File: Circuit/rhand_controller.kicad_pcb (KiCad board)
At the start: 2 copper layers, 100 x 100 mm, 37 parts, among them P1 Wall, P10 LW_ADC, P11 RU_ADC, P12 RV_ADC, P13 RW_ADC, P17 CONN_01X06, P2 CW, P3 Enable, P4 CCW, P5 LW_ADC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

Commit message: 部品割り付けの完了
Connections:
- P5 pad 2: /RHand/Joy_X -> /Joy_X
- P6 pad 2: /RHand/Joy_Y -> /Joy_Y
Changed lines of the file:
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@@
-(kicad_pcb (version 4) (host pcbnew 4.0.5)
+(kicad_pcb (version 4) (host pcbnew 4.0.6)
   (general
-    (links 121)
-    (no_connects 99)
+    (links 123)
+    (no_connects 101)
     (area 49.924999 69.924999 150.075001 170.075001)
     (thickness 1.6)
@@
     (zones 0)
     (modules 37)
-    (nets 59)
+    (nets 57)
   )
   (page A4)
@@
   (net 54 "Net-(U2-Pad26)")
   (net 55 "Net-(U3-Pad4)")
-  (net 56 /RHand/Joy_X)
-  (net 57 /RHand/Joy_Y)
-  (net 58 "Net-(SW2-Pad3)")
+  (net 56 "Net-(SW2-Pad3)")
   (net_class Default "これは標準のネット クラスです。"
     (clearance 0.2)
@@
     (add_net /LeftW)
     (add_net /NRST)
-    (add_net /RHand/Joy_X)
-    (add_net /RHand/Joy_Y)
     (add_net /RightU)
     (add_net /RightV)
@@
       (net 2 GND))
     (pad 2 thru_hole circle (at -2.5 0 90) (size 1.2 1.2) (drill 0.8) (layers *.Cu *.Mask F.SilkS)
-      (net 56 /RHand/Joy_X))
+      (net 11 /Joy_X))
     (pad 3 thru_hole circle (at -5 0 90) (size 1.2 1.2) (drill 0.8) (layers *.Cu *.Mask F.SilkS)
       (net 3 +3V3))
@@
       (net 2 GND))
     (pad 2 thru_hole circle (at -2.5 0 90) (size 1.2 1.2) (drill 0.8) (layers *.Cu *.Mask F.SilkS)
-      (net 57 /RHand/Joy_Y))
+      (net 12 /Joy_Y))
     (pad 3 thru_hole circle (at -5 0 90) (size 1.2 1.2) (drill 0.8) (layers *.Cu *.Mask F.SilkS)
       (net 3 +3V3))
@@
       (net 1 "Net-(BT1-Pad1)"))
     (pad 3 thru_hole circle (at 2.54 0 270) (size 2.2 2.2) (drill 1.016) (layers *.Cu *.Mask F.SilkS)
-      (net 58 "Net-(SW2-Pad3)"))
+      (net 56 "Net-(SW2-Pad3)"))
     (model pin_array/pins_array_5x1.wrl
       (at (xyz 0 0 0))

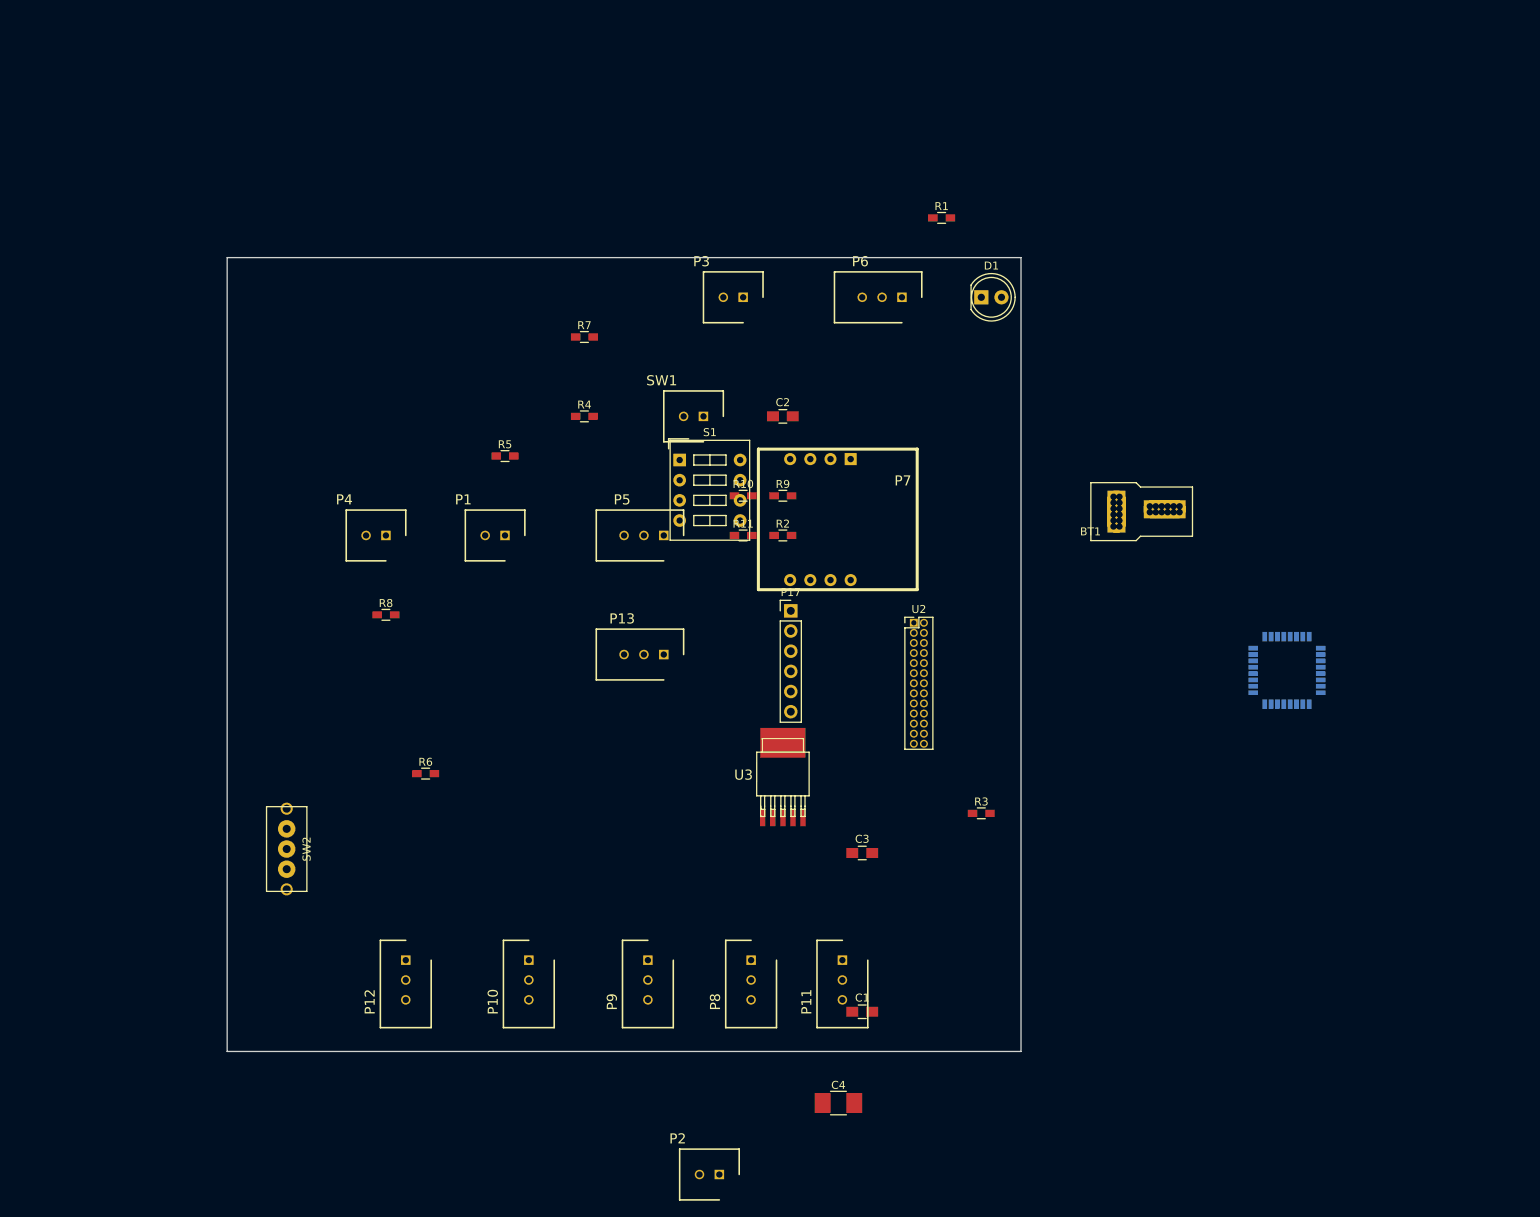
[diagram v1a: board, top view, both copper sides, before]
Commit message: 部品を基板上へ適当に配置
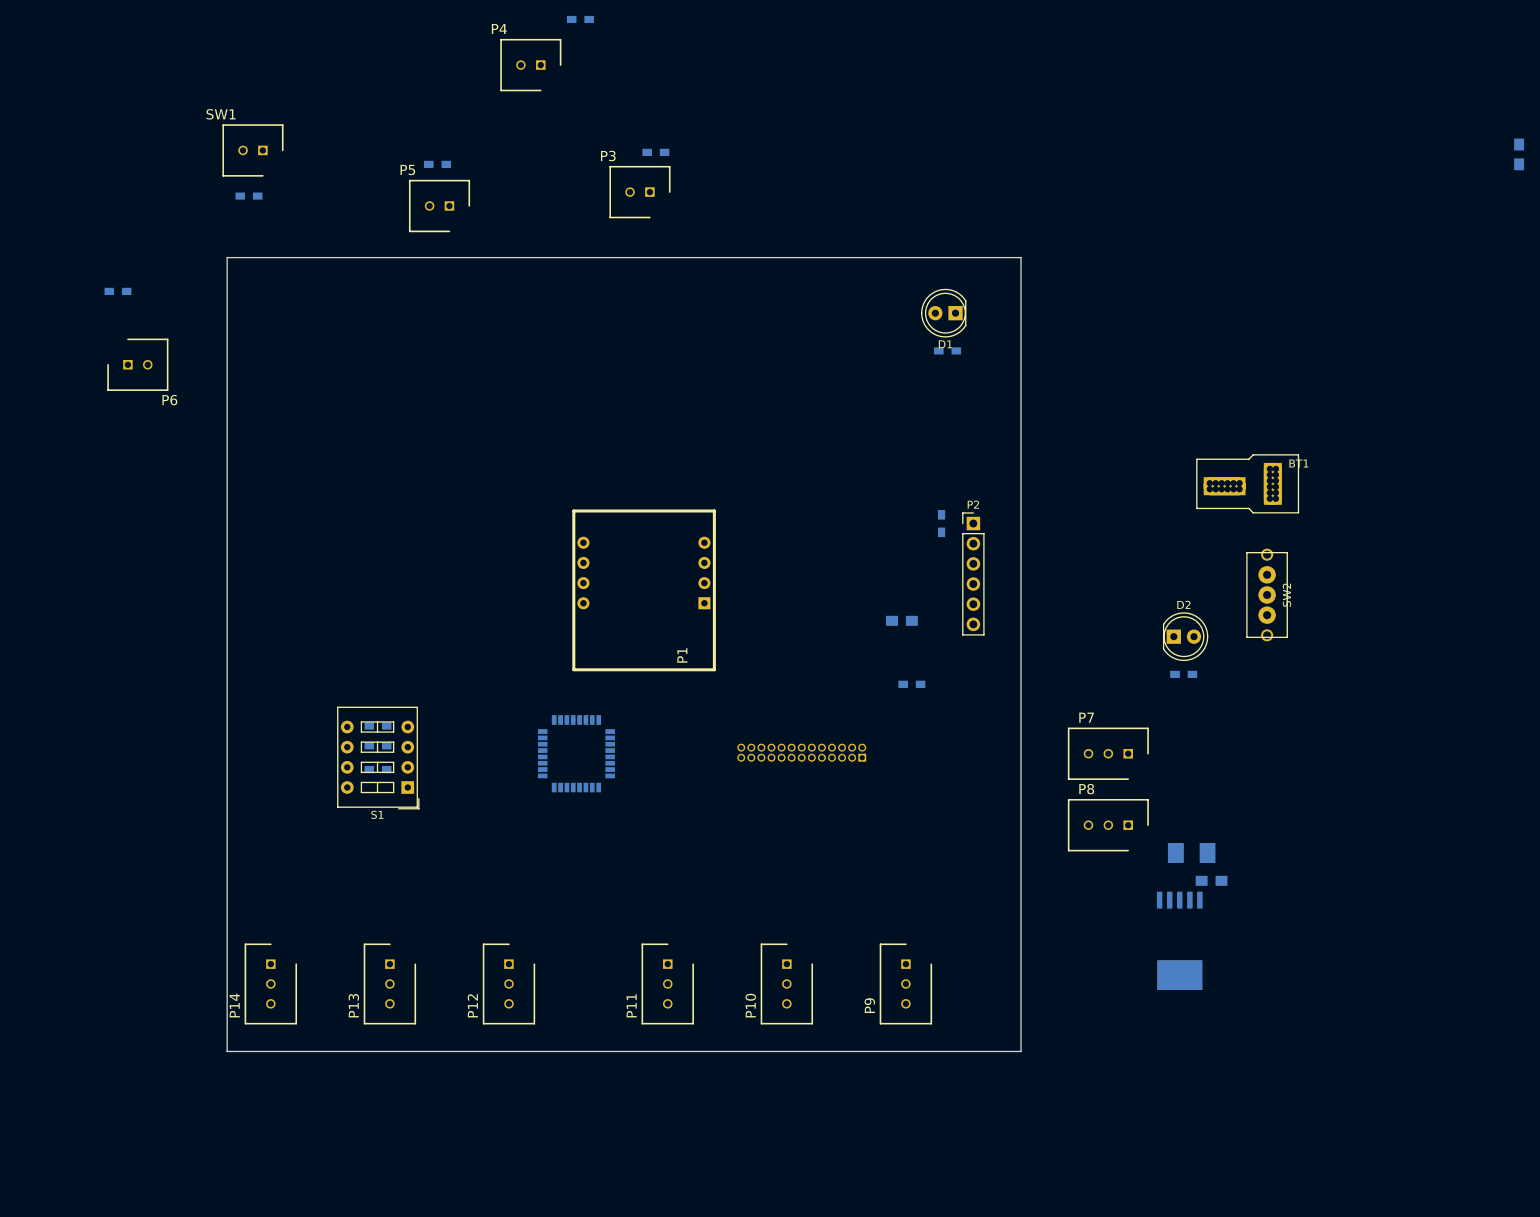
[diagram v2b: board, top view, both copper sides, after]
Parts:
- removed P17: CONN_01X06, Pin_Headers:Pin_Header_Straight_1x06_Pitch2.54mm
- added D2: LED, LEDs:LED_D5.0mm, F.Cu at (169.2, 117.8)
- added P14: RW_ADC, YASU:XA_3Pin, F.Cu at (55.5, 159.0)
- added R12: 1k, Resistors_SMD:R_0603_HandSoldering, B.Cu at (170.5, 122.5)
- BT1: value Battery -> Battery_Cell
- C1, C2, C3, C4, R10, R11, R2, R4, R6, R8, R9, U3: moved to B.Cu
- P1: value Wall -> BLUETOOTH; footprint YASU:XA_2Pin -> robocon_pcb:ESD200
- P10: value LW_ADC -> LV_ADC
- P11: value RU_ADC -> LW_ADC
- P12: value RV_ADC -> RU_ADC
- P13: value RW_ADC -> RV_ADC
- P2: value CW -> CONN_01X06; footprint YASU:XA_2Pin -> Pin_Headers:Pin_Header_Straight_1x06_Pitch2.54mm
- P3: value Enable -> Wall
- P4: value CCW -> CW
- P5: value LW_ADC -> Enable; footprint YASU:XA_3Pin -> YASU:XA_2Pin
- P6: value RW_ADC -> CCW; footprint YASU:XA_3Pin -> YASU:XA_2Pin
- P7: value BLUETOOTH -> JoyX; footprint robocon_pcb:ESD200 -> YASU:XA_3Pin
- P8: value LU_ADC -> JoyY
- P9: value LV_ADC -> LU_ADC
- R1, R3: value 1k -> 10k; moved to B.Cu
- R5, R7: value 10k -> 1k; moved to B.Cu
- U1: value STM32F042 -> IM315TRX; footprint Housings_QFP:LQFP-32_7x7mm_Pitch0.8mm -> Pin_Headers:Pin_Header_Straight_2x13_Pitch1.27mm
- U2: value IM315TRX -> STM32F042; footprint Pin_Headers:Pin_Header_Straight_2x13_Pitch1.27mm -> Housings_QFP:LQFP-32_7x7mm_Pitch0.8mm; moved to B.Cu
- moved C1 136.1 mm to (212.8, 57.0), turned to 270 degrees
- moved SW2 127.6 mm to (181.0, 112.5)
- moved P6 97.9 mm to (37.5, 83.5), turned to 180 degrees
- moved R1 95.6 mm to (69.0, 129.0), turned to 180 degrees
- moved P2 88.0 mm to (144.0, 103.5)
- moved R11 84.5 mm to (36.2, 74.2)
- moved R3 76.2 mm to (69.0, 134.5), turned to 180 degrees
- moved R8 67.4 mm to (104.0, 56.8), turned to 180 degrees
- moved R9 65.2 mm to (94.5, 40.0)
- moved SW1 64.8 mm to (54.5, 56.5)
- moved P4 62.4 mm to (89.5, 45.8)
- moved R6 62.3 mm to (136.2, 123.8), turned to 180 degrees
- moved R2 57.5 mm to (69.0, 131.5), turned to 180 degrees
- moved R5 57.3 mm to (140.8, 81.8), turned to 180 degrees
- moved R10 56.8 mm to (76.5, 58.2), turned to 180 degrees
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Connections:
- C1 pad 1: +3V3 -> GND
- C1 pad 2: GND -> +3V3
- C2 pad 1: GND -> +3V3
- C2 pad 2: +3V3 -> GND
- P1 pad 2: /Wall -> +3V3
- P10 pad 2: /LeftW -> /LeftV
- P11 pad 2: /RightV -> /LeftW
- P12 pad 2: /RightW -> /RightU
- P13 pad 2: /RightU -> /RightV
- P2 pad 1: GND -> Net-(P2-Pad1)
- P2 pad 2: /CW -> /SWCLK
- P3 pad 2: /Enable -> /Wall
- P4 pad 2: /CCW -> /CW
- P5 pad 2: /Joy_X -> /Enable
- P6 pad 2: /Joy_Y -> /CCW
- P7 pad 2: +3V3 -> /Joy_X
- P7 pad 3: Net-(P7-Pad3) -> +3V3
- P8 pad 2: /LeftU -> /Joy_Y
- P9 pad 2: /LeftV -> /LeftU
- R1 pad 1: Net-(D1-Pad1) -> /DSW_B2
- R10 pad 1: /DSW_B1 -> +3V3
- R10 pad 2: GND -> /Enable
- R11 pad 1: /DSW_B2 -> +3V3
- R11 pad 2: GND -> /CCW
- R2 pad 1: GND -> /DSW_B1
- R2 pad 2: Net-(R2-Pad2) -> GND
- R3 pad 1: +3V3 -> /DSW_B0
- R3 pad 2: /NRST -> GND
- R5 pad 1: +3V3 -> Net-(D1-Pad1)
- R5 pad 2: /Wall -> GND
- R6 pad 1: +3V3 -> GND
- R6 pad 2: /CW -> Net-(R6-Pad2)
- R7 pad 2: /Enable -> /NRST
- R8 pad 2: /CCW -> /Wall
- R9 pad 1: /DSW_B0 -> +3V3
- R9 pad 2: GND -> /CW
- U1 pad 1: +3V3 -> /busy
- U1 pad 10: /LeftU -> Net-(U1-Pad10)
- U1 pad 11: /LeftV -> Net-(U1-Pad11)
- U1 pad 12: /LeftW -> Net-(U1-Pad12)
- U1 pad 13: /RightU -> Net-(U1-Pad13)
- U1 pad 14: /RightV -> Net-(U1-Pad14)
- U1 pad 15: /RightW -> Net-(U1-Pad15)
- U1 pad 16: GND -> Net-(U1-Pad16)
- U1 pad 18: /CW -> GND
- U1 pad 19: /CCW -> GND
- U1 pad 2: /Wall -> Net-(U1-Pad2)
- U1 pad 20: /DSW_B0 -> Net-(U1-Pad20)
- U1 pad 21: /DSW_B1 -> Net-(D1-Pad2)
- U1 pad 22: /DSW_B2 -> Net-(U1-Pad22)
- U1 pad 23: /SWDIO -> +3V3
- U1 pad 24: /SWCLK -> GND
- U1 pad 25: Net-(R4-Pad2) -> /reset315
- U1 pad 26: /SWO -> Net-(U1-Pad26)
- U1 pad 3: /Enable -> Net-(U1-Pad3)
- U1 pad 4: /NRST -> Net-(U1-Pad4)
- U1 pad 5: +3V3 -> Net-(U1-Pad5)
- U1 pad 6: /Joy_X -> /315MHz_RXD
- U1 pad 7: /Joy_Y -> /315MHz_TXD
- U1 pad 8: /315MHz_RXD -> Net-(U1-Pad8)
- U1 pad 9: /315MHz_TXD -> Net-(U1-Pad9)
- U2 pad 1: /busy -> +3V3
- U2 pad 10: Net-(U2-Pad10) -> /LeftU
- U2 pad 11: Net-(U2-Pad11) -> /LeftV
- U2 pad 12: Net-(U2-Pad12) -> /LeftW
- U2 pad 13: Net-(U2-Pad13) -> /RightU
- U2 pad 14: Net-(U2-Pad14) -> /RightV
- U2 pad 15: Net-(U2-Pad15) -> /RightW
- U2 pad 16: Net-(U2-Pad16) -> GND
- U2 pad 18: GND -> /CW
- U2 pad 19: GND -> /CCW
- U2 pad 2: Net-(U2-Pad2) -> /Wall
- U2 pad 20: Net-(U2-Pad20) -> /DSW_B0
- U2 pad 21: Net-(D1-Pad2) -> /DSW_B1
- U2 pad 22: Net-(U2-Pad22) -> /DSW_B2
- U2 pad 23: +3V3 -> /SWDIO
- U2 pad 24: GND -> /SWCLK
- U2 pad 25: /reset315 -> Net-(R4-Pad2)
- U2 pad 26: Net-(U2-Pad26) -> /SWO
- U2 pad 3: Net-(U2-Pad3) -> /Enable
- U2 pad 4: Net-(U2-Pad4) -> /NRST
- U2 pad 5: Net-(U2-Pad5) -> +3V3
- U2 pad 6: /315MHz_RXD -> /Joy_X
- U2 pad 7: /315MHz_TXD -> /Joy_Y
- U2 pad 8: Net-(U2-Pad8) -> /315MHz_RXD
- U2 pad 9: Net-(U2-Pad9) -> /315MHz_TXD

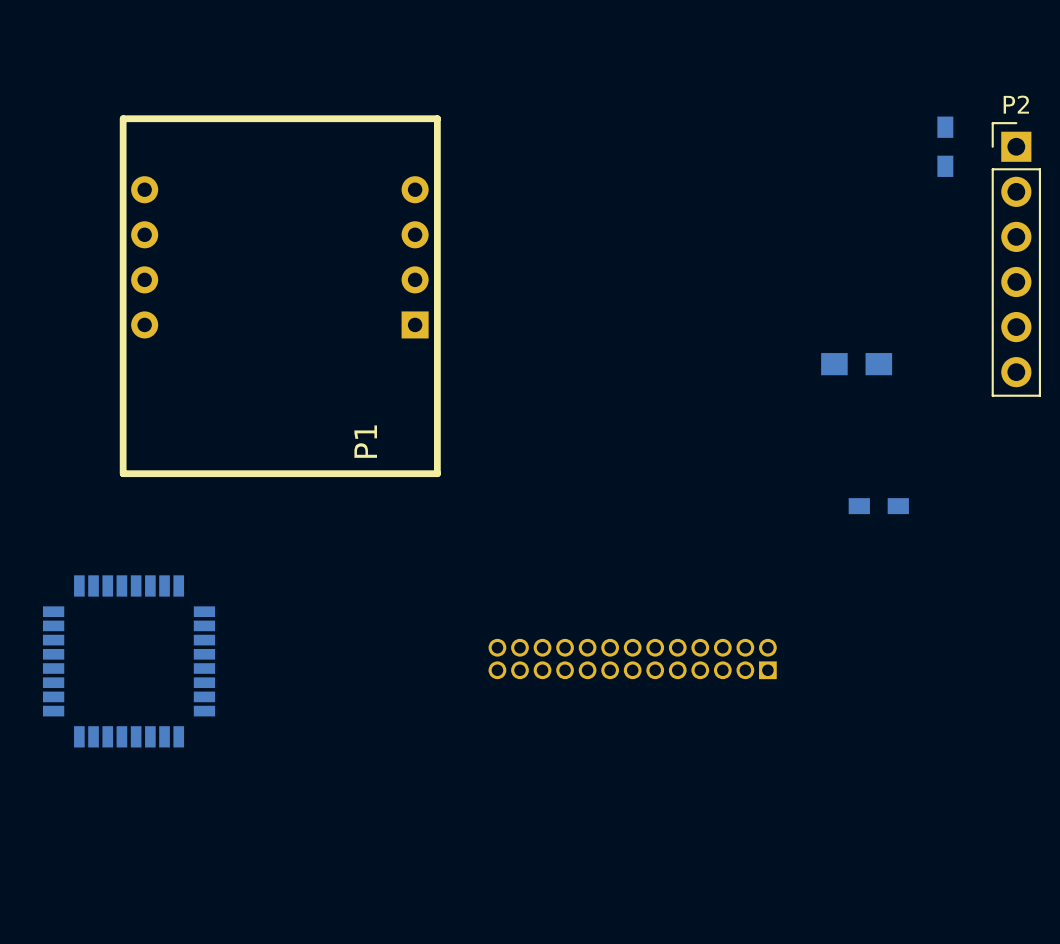
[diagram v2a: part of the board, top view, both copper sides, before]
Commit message: ピンヘッダを表面実装へ
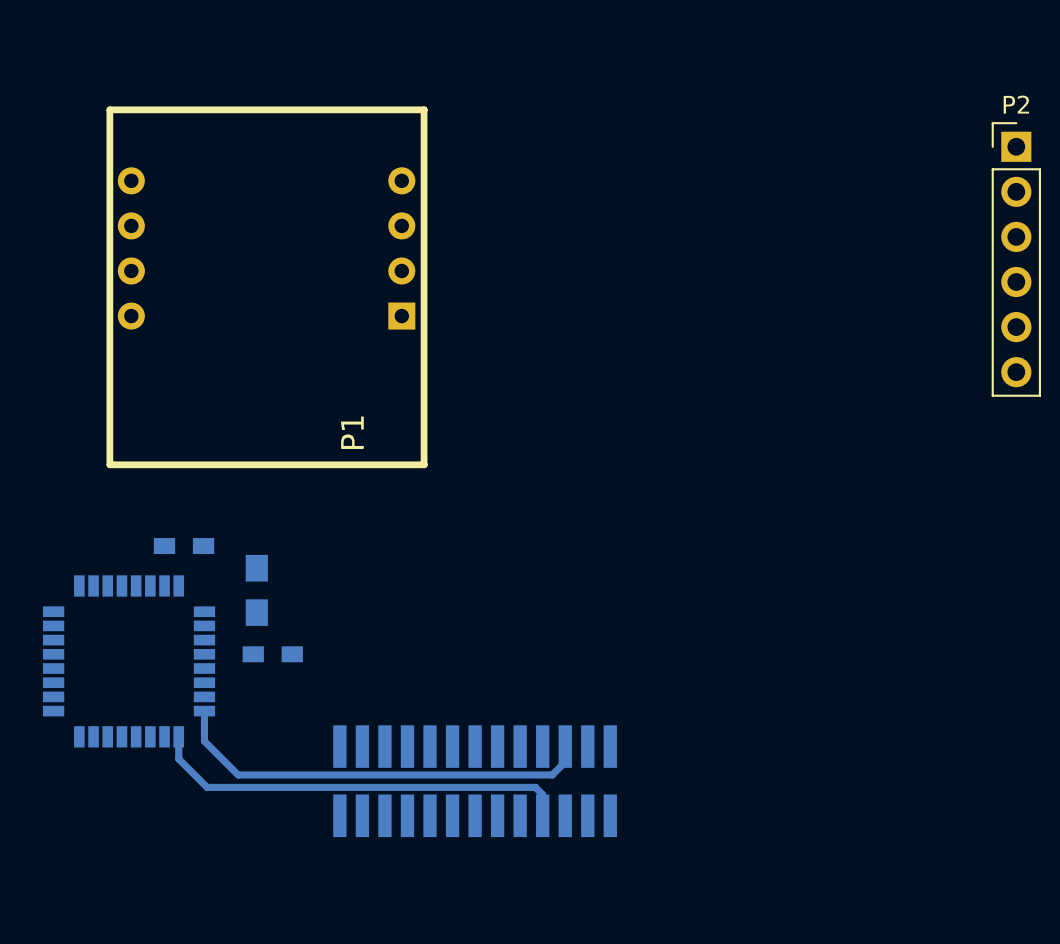
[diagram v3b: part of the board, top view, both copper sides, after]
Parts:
- U1: footprint Pin_Headers:Pin_Header_Straight_2x13_Pitch1.27mm -> Pin_Headers:Pin_Header_Straight_2x13_Pitch1.27mm_SMD
- moved R7 47.5 mm to (102.1, 132.1), turned to 180 degrees
- moved R6 39.2 mm to (97.1, 126.0)
- moved C2 36.1 mm to (101.2, 128.5), turned to 90 degrees
- moved U1 17.6 mm to (113.5, 139.2)
- moved P1 0.90 mm to (101.8, 110.5)
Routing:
- net /315MHz_RXD: track 0.00 -> 24.0 mm
- net /315MHz_TXD: track 0.00 -> 23.8 mm
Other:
- net class Default: clearance 0.2 -> 0.1; trace_width 0.25 -> 0.5; via_dia 0.6 -> 1.2; via_drill 0.4 -> 0.8
- rule trace_clearance: 0.2 -> 0.1
